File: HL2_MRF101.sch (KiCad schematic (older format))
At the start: 213 parts, among them J1 Antenna, J10 DB1, J2 HL2, J3 RF3, J4 RF1, J5 RCJ-041, J6 50VDC, J7 12V, J8 Fan, J9 HL2_12V, K1 EC2-3NU, K10 EC2-3NU, K11 EC2-3NU, K12 EC2-3NU, K13 EC2-3NU, K2 EC2-3NU, K3 EC2-3NU, K4 EC2-3NU, K5 EC2-3NU, K6 EC2-3NU, K7 EC2-3NU, K8 EC2-3NU, K9 EC2-3NU, Q1 MRF101AN, Q2 2N7002, Q3 IRLML6402, Q4 DTC144E, T1 Coupler, T2 Coupler, T3 744851330, U1 MCP6282E/MS, U2 MAX11613, U3 MCP23008, U4 ULN2003, U5 LM35-NEB, U6 MCP4561, U7 INA193

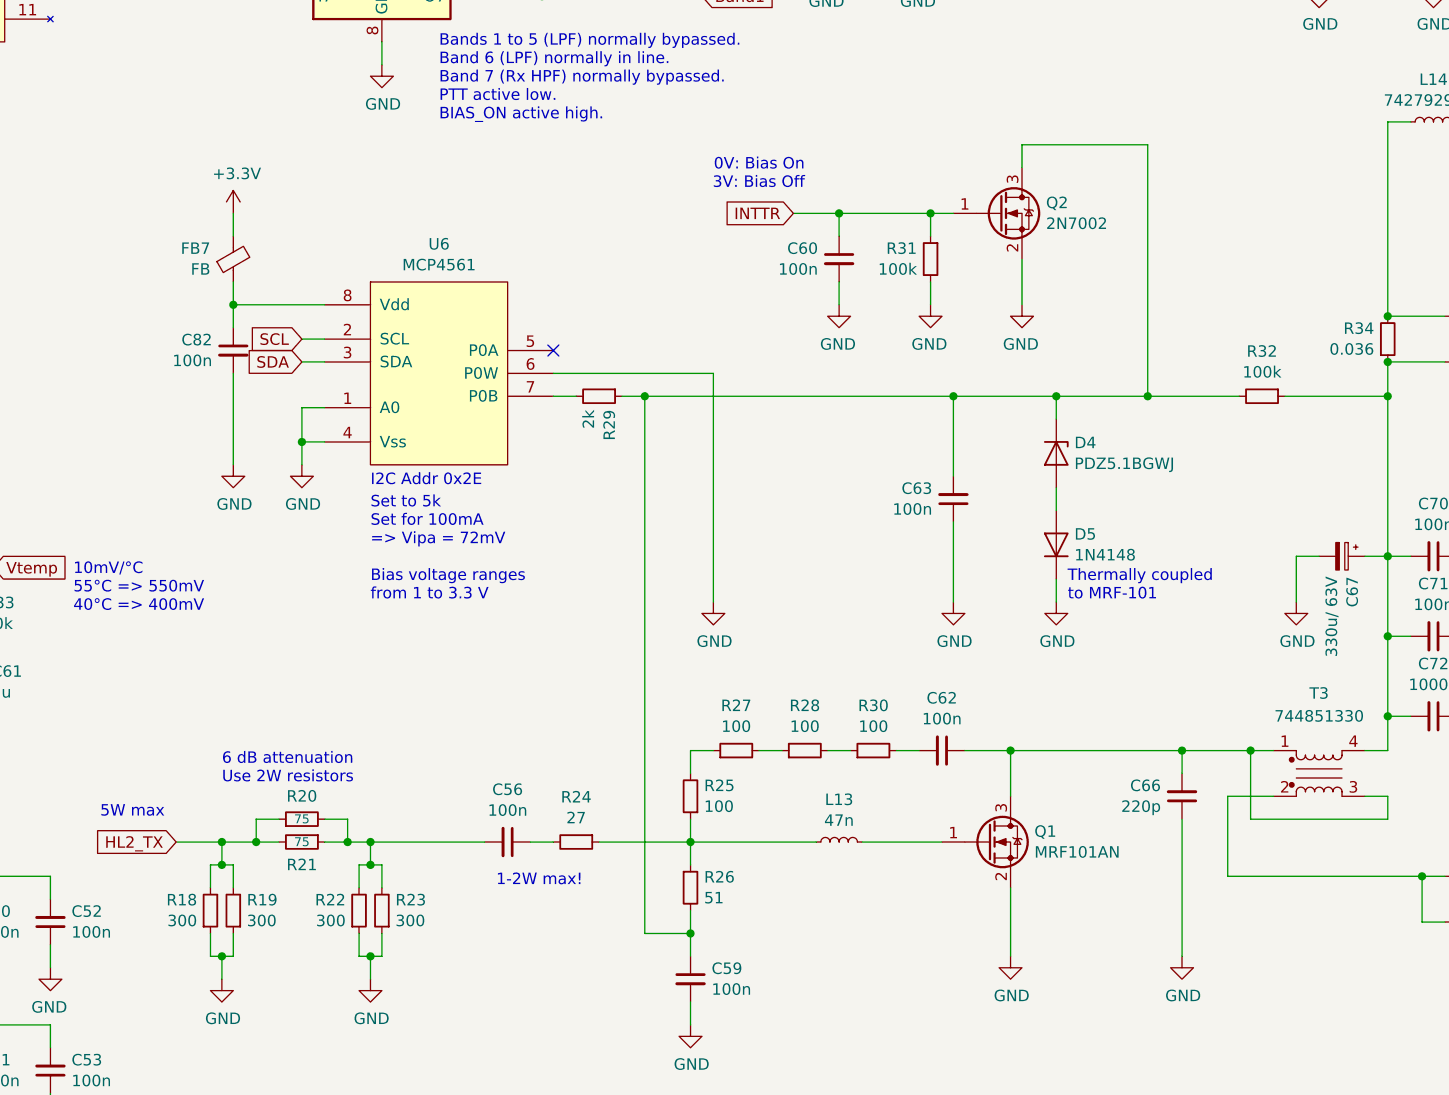
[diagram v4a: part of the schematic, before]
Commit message: Reworked bias circuit, again.
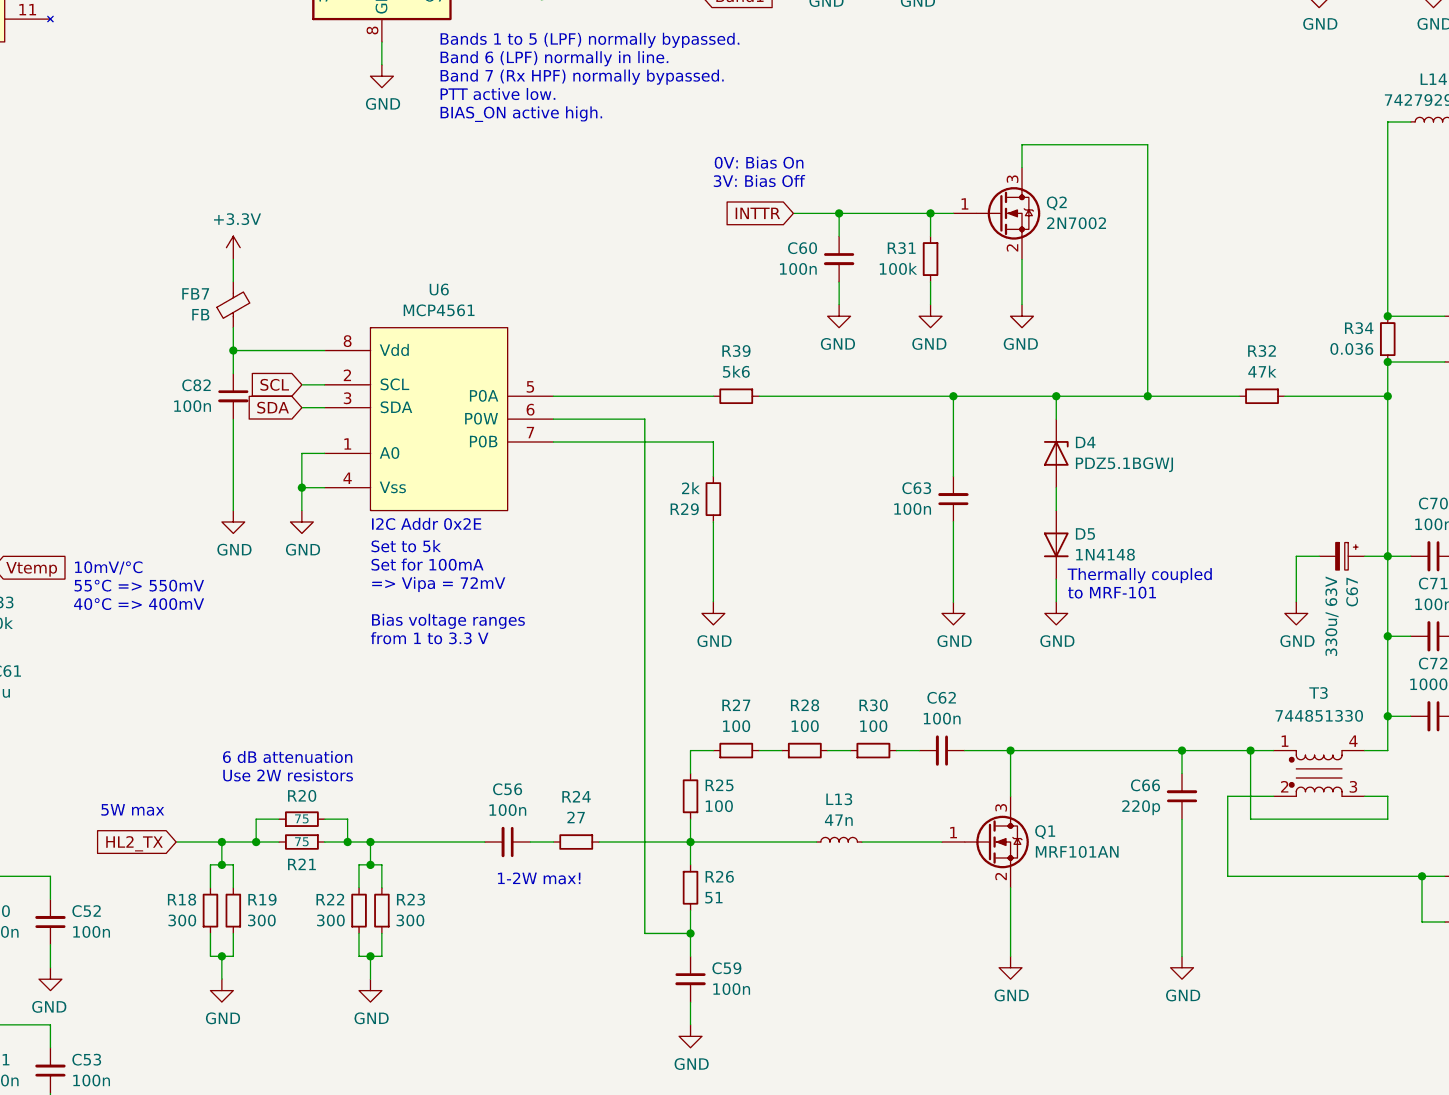
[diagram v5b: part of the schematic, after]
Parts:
- added R39: 5k6, Resistor_SMD:R_0805_2012Metric, symbol HL2_MRF101-rescue:R_Small-Device
- R32: value 100k -> 47k
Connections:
- net GND: now also R29.1; no longer U6.6 (P0W)
- net at C63.2, D4.1 (K), Q2.3 (D)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: now also R39.1; no longer C59.1, R26.2, R29.1
- net at U6.5 (P0A): now also R39.2
- new net: C59.1, R26.2, U6.6 (P0W)
- no-connect marks 10 -> 9
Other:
- moved on the sheet: C82, FB7, R29, U6
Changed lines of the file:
@@
 P 13450 3950
 F 0 "R32" V 13254 3950 50  0000 C CNN
-F 1 "100k" V 13345 3950 50  0000 C CNN
+F 1 "47k" V 13345 3950 50  0000 C CNN
 F 2 "Resistor_SMD:R_0805_2012Metric" H 13450 3950 50  0001 C CNN
 F 3 "~" H 13450 3950 50  0001 C CNN
@@
 Wire Wire Line
 	13900 4650 14000 4650
-Text Notes 9550 4850 0    50   ~ 0
+Text Notes 9550 5050 0    50   ~ 0
 Set to 5k\nSet for 100mA\n=> Vipa = 72mV\n\nBias voltage ranges\nfrom 1 to 3.3 V
 Text Notes 10100 6100 0    50   ~ 0
@@
 L HL2-MRF101:MCP4561 U6
 U 1 1 6200A830
-P 9850 3850
-F 0 "U6" H 9850 4415 50  0000 C CNN
-F 1 "MCP4561" H 9850 4324 50  0000 C CNN
-F 2 "Package_SO:MSOP-8_3x3mm_P0.65mm" H 9650 5500 50  0001 C CNN
-F 3 "" H 9650 5500 50  0001 C CNN
-	1    9850 3850
+P 9850 4050
+F 0 "U6" H 9850 4615 50  0000 C CNN
+F 1 "MCP4561" H 9850 4524 50  0000 C CNN
+F 2 "Package_SO:MSOP-8_3x3mm_P0.65mm" H 9650 5700 50  0001 C CNN
+F 3 "" H 9650 5700 50  0001 C CNN
+	1    9850 4050
 	1    0    0    -1
 $EndComp
-Text GLabel 9250 3700 0    50   Input ~ 0
+Text GLabel 9250 3900 0    50   Input ~ 0
 SCL
-Text GLabel 9250 3800 0    50   Input ~ 0
+Text GLabel 9250 4000 0    50   Input ~ 0
 SDA
 Wire Wire Line
-	9350 3800 9250 3800
+	9350 4000 9250 4000
 Wire Wire Line
-	9350 3700 9250 3700
+	9350 3900 9250 3900
 Wire Wire Line
-	8950 3550 9350 3550
+	8950 3750 9350 3750
 $Comp
 L HL2_MRF101-rescue:C_Small-Device C82
 U 1 1 6244D31F
-P 8950 3750
-F 0 "C82" H 9042 3796 50  0000 L CNN
-F 1 "100n" H 9042 3705 50  0000 L CNN
-F 2 "Capacitor_SMD:C_0805_2012Metric" H 8950 3750 50  0001 C CNN
-F 3 "~" H 8950 3750 50  0001 C CNN
-	1    8950 3750
+P 8950 3950
+F 0 "C82" H 9042 3996 50  0000 L CNN
+F 1 "100n" H 9042 3905 50  0000 L CNN
+F 2 "Capacitor_SMD:C_0805_2012Metric" H 8950 3950 50  0001 C CNN
+F 3 "~" H 8950 3950 50  0001 C CNN
+	1    8950 3950
 	-1   0    0    -1
 $EndComp
 Wire Wire Line
-	8950 3550 8950 3650
+	8950 3750 8950 3850
 $Comp
 L power:+3.3V #PWR0104
 U 1 1 624EB2A7
-P 8950 3150
-F 0 "#PWR0104" H 8950 3000 50  0001 C CNN
-F 1 "+3.3V" H 8965 3323 50  0000 C CNN
-F 2 "" H 8950 3150 50  0001 C CNN
-F 3 "" H 8950 3150 50  0001 C CNN
-	1    8950 3150
+P 8950 3350
+F 0 "#PWR0104" H 8950 3200 50  0001 C CNN
+F 1 "+3.3V" H 8965 3523 50  0000 C CNN
+F 2 "" H 8950 3350 50  0001 C CNN
+F 3 "" H 8950 3350 50  0001 C CNN
+	1    8950 3350
 	1    0    0    -1
 $EndComp
@@
 L HL2_MRF101-rescue:Ferrite_Bead_Small-device FB7
 U 1 1 624EB2B1
-P 8950 3350
-F 0 "FB7" H 8850 3304 50  0000 R CNN
-F 1 "FB" H 8850 3395 50  0000 R CNN
-F 2 "Inductor_SMD:L_0805_2012Metric" V 8880 3350 50  0001 C CNN
-F 3 "~" H 8950 3350 50  0001 C CNN
-	1    8950 3350
+P 8950 3550
+F 0 "FB7" H 8850 3504 50  0000 R CNN
+F 1 "FB" H 8850 3595 50  0000 R CNN
+F 2 "Inductor_SMD:L_0805_2012Metric" V 8880 3550 50  0001 C CNN
+F 3 "~" H 8950 3550 50  0001 C CNN
+	1    8950 3550
 	1    0    0    1
 $EndComp
 Wire Wire Line
-	8950 3150 8950 3250
+	8950 3350 8950 3450
 Wire Wire Line
-	8950 3450 8950 3550
+	8950 3650 8950 3750
 $Comp
 L power:GND #PWR0112
 U 1 1 62627FA1
-P 9250 4250
-F 0 "#PWR0112" H 9250 4000 50  0001 C CNN
-F 1 "GND" H 9255 4077 50  0000 C CNN
-F 2 "" H 9250 4250 50  0001 C CNN
-F 3 "" H 9250 4250 50  0001 C CNN
-	1    9250 4250
+P 9250 4450
+F 0 "#PWR0112" H 9250 4200 50  0001 C CNN
+F 1 "GND" H 9255 4277 50  0000 C CNN
+F 2 "" H 9250 4450 50  0001 C CNN
+F 3 "" H 9250 4450 50  0001 C CNN
+	1    9250 4450
 	1    0    0    -1
 $EndComp
 Wire Wire Line
-	9350 4150 9250 4150
+	9350 4350 9250 4350
 Wire Wire Line
-	9250 4150 9250 4250
+	9250 4350 9250 4450
 $Comp
 L power:GND #PWR0111
 U 1 1 626C7205
-P 8950 4250
-F 0 "#PWR0111" H 8950 4000 50  0001 C CNN
-F 1 "GND" H 8955 4077 50  0000 C CNN
-F 2 "" H 8950 4250 50  0001 C CNN
-F 3 "" H 8950 4250 50  0001 C CNN
-	1    8950 4250
+P 8950 4450
+F 0 "#PWR0111" H 8950 4200 50  0001 C CNN
+F 1 "GND" H 8955 4277 50  0000 C CNN
+F 2 "" H 8950 4450 50  0001 C CNN
+F 3 "" H 8950 4450 50  0001 C CNN
+	1    8950 4450
 	1    0    0    -1
 $EndComp
 Wire Wire Line
-	8950 3850 8950 4250
-Text Notes 9550 4350 0    50   ~ 0
+	8950 4050 8950 4450
+Text Notes 9550 4550 0    50   ~ 0
 I2C Addr 0x2E
 Wire Wire Line
-	9350 4000 9250 4000
+	9350 4200 9250 4200
 Wire Wire Line
-	9250 4000 9250 4150
-Connection ~ 9250 4150
-Connection ~ 8950 3550
+	9250 4200 9250 4350
+Connection ~ 9250 4350
+Connection ~ 8950 3750
 Text Notes 14450 3550 0    50   ~ 0
 4A => 144mV
@@
 L HL2_MRF101-rescue:R_Small-Device R29
 U 1 1 5E0BF37A
-P 10550 3950
-F 0 "R29" H 10609 3996 50  0000 L CNN
-F 1 "2k" H 10609 3905 50  0000 L CNN
-F 2 "Resistor_SMD:R_0805_2012Metric" H 10550 3950 50  0001 C CNN
-F 3 "~" H 10550 3950 50  0001 C CNN
-	1    10550 3950
-	0    1    1    0
+P 11050 4400
+F 0 "R29" H 11109 4446 50  0000 L CNN
+F 1 "2k" H 11109 4355 50  0000 L CNN
+F 2 "Resistor_SMD:R_0805_2012Metric" H 11050 4400 50  0001 C CNN
+F 3 "~" H 11050 4400 50  0001 C CNN
+	1    11050 4400
+	-1   0    0    1
 $EndComp
 Text GLabel 1000 8950 2    50   Input ~ 0
@@
 Wire Wire Line
 	1750 10350 1850 10350
-NoConn ~ 10350 3750
-Wire Wire Line
-	10350 3950 10450 3950
-Wire Wire Line
-	10750 6300 10750 3950
-Wire Wire Line
-	10750 3950 10650 3950
-Wire Wire Line
-	10750 3950 12100 3950
-Connection ~ 10750 3950
-Connection ~ 12100 3950
-Wire Wire Line
-	10350 3850 11050 3850
-Wire Wire Line
-	11050 3850 11050 4850
 $Comp
-L power:GND #PWR?
+L power:GND #PWR061
 U 1 1 63E68A3C
 P 11050 4850
-F 0 "#PWR?" H 11050 4600 50  0001 C CNN
+F 0 "#PWR061" H 11050 4600 50  0001 C CNN
 F 1 "GND" H 11055 4677 50  0000 C CNN
 F 2 "" H 11050 4850 50  0001 C CNN
@@
 	1    0    0    -1
 $EndComp
+$Comp
+L HL2_MRF101-rescue:R_Small-Device R39
+U 1 1 5E3E3EE6
+P 11150 3950
+F 0 "R39" V 10954 3950 50  0000 C CNN
+F 1 "5k6" V 11045 3950 50  0000 C CNN
+F 2 "Resistor_SMD:R_0805_2012Metric" H 11150 3950 50  0001 C CNN
+F 3 "~" H 11150 3950 50  0001 C CNN
+	1    11150 3950
+	0    1    1    0
+$EndComp
+Wire Wire Line
+	10350 4150 11050 4150
+Wire Wire Line
+	11050 4150 11050 4300
+Wire Wire Line
+	11050 4500 11050 4850
+Wire Wire Line
+	11250 3950 12100 3950
+Connection ~ 12100 3950
+Wire Wire Line
+	11050 3950 10350 3950
+Wire Wire Line
+	10750 6300 10750 4050
+Wire Wire Line
+	10750 4050 10350 4050
 $EndSCHEMATC

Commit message: Impedance Adjustment started
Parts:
- added F?: Fuse_Small, symbol Device:Fuse_Small
- C84, C85: symbol device:C_Small -> HL2_MRF101-rescue:C_Small-device
- D6: symbol diode:1N4148W -> HL2_MRF101-rescue:1N4148W-diode
- FB10, FB11, FB12, FB13, FB14, FB15, FB16, FB17, FB18, FB9: symbol device:Ferrite_Bead_Small -> HL2_MRF101-rescue:Ferrite_Bead_Small-device
- J10: symbol conn:Conn_01x06 -> HL2_MRF101-rescue:Conn_01x06-conn
- Q3: symbol device:Q_PMOS_GSD -> HL2_MRF101-rescue:Q_PMOS_GSD-device
- Q4: symbol transistors:DTC144E -> HL2_MRF101-rescue:DTC144E-transistors
- R10, R5: value 56k -> 100k
- R11, R4: value 100k -> 56k
- R16, R17, R36, R37, R38: symbol device:R_Small -> HL2_MRF101-rescue:R_Small-device
- U2: value MAX11613 -> MAX11645
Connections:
- net at J6.1 (Pin_1): now also F?.1; no longer L14.1
- new net: F?.2, L14.1
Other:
- moved on the sheet: L14
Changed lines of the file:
@@
 P 12400 8200
 F 0 "R10" V 12204 8200 50  0000 C CNN
-F 1 "56k" V 12295 8200 50  0000 C CNN
+F 1 "100k" V 12295 8200 50  0000 C CNN
 F 2 "Resistor_SMD:R_0805_2012Metric" H 12400 8200 50  0001 C CNN
 F 3 "~" H 12400 8200 50  0001 C CNN
@@
 P 12600 8400
 F 0 "R11" H 12541 8354 50  0000 R CNN
-F 1 "100k" H 12541 8445 50  0000 R CNN
+F 1 "56k" H 12541 8445 50  0000 R CNN
 F 2 "Resistor_SMD:R_0805_2012Metric" H 12600 8400 50  0001 C CNN
 F 3 "~" H 12600 8400 50  0001 C CNN
@@
 P 9350 8200
 F 0 "R5" V 9154 8200 50  0000 C CNN
-F 1 "56k" V 9245 8200 50  0000 C CNN
+F 1 "100k" V 9245 8200 50  0000 C CNN
 F 2 "Resistor_SMD:R_0805_2012Metric" H 9350 8200 50  0001 C CNN
 F 3 "~" H 9350 8200 50  0001 C CNN
@@
 P 9150 8400
 F 0 "R4" H 9091 8354 50  0000 R CNN
-F 1 "100k" H 9091 8445 50  0000 R CNN
+F 1 "56k" H 9091 8445 50  0000 R CNN
 F 2 "Resistor_SMD:R_0805_2012Metric" H 9150 8400 50  0001 C CNN
 F 3 "~" H 9150 8400 50  0001 C CNN
@@
 	14550 2750 14300 2750
 $Comp
-L HL2_MRF101-rescue:L_Small-Device L14
-U 1 1 63DACD97
-P 14200 2750
-F 0 "L14" V 14385 2750 50  0000 C CNN
-F 1 "7427929112" V 14294 2750 50  0000 C CNN
-F 2 "n2adr:SignalCommunications-WE-PF_7427929XXX" H 14200 2750 50  0001 C CNN
-F 3 "~" H 14200 2750 50  0001 C CNN
-	1    14200 2750
-	0    1    -1   0
-$EndComp
-$Comp
 L HL2_MRF101-rescue:Conn_01x02-Connector_Generic J6
 U 1 1 63DAB1DA
@@
 	1    0    0    -1
 $EndComp
-Wire Wire Line
-	14000 2750 14100 2750
 $Comp
 L power:GND #PWR0113
@@
 P 14700 1600
 F 0 "U2" H 14700 1187 50  0000 C CNN
-F 1 "MAX11613" H 14700 1278 49  0000 C CNN
+F 1 "MAX11645" H 14700 1278 49  0000 C CNN
 F 2 "n2adr:MAX11613" H 14700 1125 50  0001 C CNN
 F 3 "DOCUMENTATION" H 14700 1300 50  0001 C CNN
@@
 	14000 3950 14000 4650
 Connection ~ 14000 3950
-Wire Wire Line
-	14000 3600 14000 2750
-Connection ~ 14000 3600
 $Comp
-L device:Ferrite_Bead_Small FB10
+L HL2_MRF101-rescue:Ferrite_Bead_Small-device FB10
 U 1 1 5E39790B
 P 5950 1600
@@
 	6050 1600 6150 1600
 $Comp
-L device:Ferrite_Bead_Small FB12
+L HL2_MRF101-rescue:Ferrite_Bead_Small-device FB12
 U 1 1 5E4400FC
 P 5950 2900
@@
 	6150 2900 6050 2900
 $Comp
-L device:Ferrite_Bead_Small FB14
+L HL2_MRF101-rescue:Ferrite_Bead_Small-device FB14
 U 1 1 5E4E8E6D
 P 5950 4200
@@
 	6050 4200 6150 4200
 $Comp
-L device:Ferrite_Bead_Small FB16
+L HL2_MRF101-rescue:Ferrite_Bead_Small-device FB16
 U 1 1 5E5925AB
 P 5950 5500
@@
 	6150 5500 6050 5500
 $Comp
-L device:Ferrite_Bead_Small FB18
+L HL2_MRF101-rescue:Ferrite_Bead_Small-device FB18
 U 1 1 5E63C014
 P 5950 6800
@@
 Connection ~ 5450 6700
 $Comp
-L device:Ferrite_Bead_Small FB17
+L HL2_MRF101-rescue:Ferrite_Bead_Small-device FB17
 U 1 1 5E9A3A71
 P 1000 6800
@@
 	800  6800 900  6800
 $Comp
-L device:Ferrite_Bead_Small FB15
+L HL2_MRF101-rescue:Ferrite_Bead_Small-device FB15
 U 1 1 5EAFA782
 P 1000 5500
@@
 	800  5500 900  5500
 $Comp
-L device:Ferrite_Bead_Small FB13
+L HL2_MRF101-rescue:Ferrite_Bead_Small-device FB13
 U 1 1 5ECFC9ED
 P 1000 4200
@@
 	800  4200 900  4200
 $Comp
-L device:Ferrite_Bead_Small FB11
+L HL2_MRF101-rescue:Ferrite_Bead_Small-device FB11
 U 1 1 5EE55DAE
 P 1000 2900
@@
 	800  2900 900  2900
 $Comp
-L device:Ferrite_Bead_Small FB9
+L HL2_MRF101-rescue:Ferrite_Bead_Small-device FB9
 U 1 1 5F107944
 P 1000 1600
@@
 	900  9950 2950 9950
 $Comp
-L device:R_Small R36
+L HL2_MRF101-rescue:R_Small-device R36
 U 1 1 5F471469
 P 1950 10350
@@
 $EndComp
 $Comp
-L device:R_Small R38
+L HL2_MRF101-rescue:R_Small-device R38
 U 1 1 5F4733D9
 P 2150 10550
@@
 $EndComp
 $Comp
-L device:R_Small R37
+L HL2_MRF101-rescue:R_Small-device R37
 U 1 1 5F47390A
 P 1750 10550
@@
 FWD_DET
 $Comp
-L transistors:DTC144E Q4
+L HL2_MRF101-rescue:DTC144E-transistors Q4
 U 1 1 5FE35199
 P 9550 10400
@@
 $EndComp
 $Comp
-L device:Q_PMOS_GSD Q3
+L HL2_MRF101-rescue:Q_PMOS_GSD-device Q3
 U 1 1 5FF9F9AC
 P 10450 10100
@@
 	8450 1500 8450 1400
 $Comp
-L device:C_Small C85
+L HL2_MRF101-rescue:C_Small-device C85
 U 1 1 604A1A52
 P 10550 10600
@@
 	10150 10100 10250 10100
 $Comp
-L device:C_Small C84
+L HL2_MRF101-rescue:C_Small-device C84
 U 1 1 60D3909C
 P 10150 10400
@@
 Connection ~ 10150 10100
 $Comp
-L device:R_Small R17
+L HL2_MRF101-rescue:R_Small-device R17
 U 1 1 60EABC72
 P 9950 10100
@@
 	10150 10500 10150 10800
 $Comp
-L device:R_Small R16
+L HL2_MRF101-rescue:R_Small-device R16
 U 1 1 616A8DF0
 P 10350 9800
@@
 $EndComp
 $Comp
-L diode:1N4148W D6
+L HL2_MRF101-rescue:1N4148W-diode D6
 U 1 1 618D1626
 P 10850 10600
@@
 	9650 10100 9850 10100
 $Comp
-L conn:Conn_01x06 J10
+L HL2_MRF101-rescue:Conn_01x06-conn J10
 U 1 1 62688D8F
 P 8400 10400
@@
 Wire Wire Line
 	10750 4050 10350 4050
+$Comp
+L Device:Fuse_Small F?
+U 1 1 5E4932D6
+P 14200 2750
+F 0 "F?" H 14200 2565 50  0000 C CNN
+F 1 "Fuse_Small" H 14200 2656 50  0000 C CNN
+F 2 "" H 14200 2750 50  0001 C CNN
+F 3 "~" H 14200 2750 50  0001 C CNN
+	1    14200 2750
+	-1   0    0    1
+$EndComp
+$Comp
+L HL2_MRF101-rescue:L_Small-Device L14
+U 1 1 63DACD97
+P 14000 3050
+F 0 "L14" V 14185 3050 50  0000 C CNN
+F 1 "7427929112" V 14094 3050 50  0000 C CNN
+F 2 "n2adr:SignalCommunications-WE-PF_7427929XXX" H 14000 3050 50  0001 C CNN
+F 3 "~" H 14000 3050 50  0001 C CNN
+	1    14000 3050
+	-1   0    0    -1
+$EndComp
+Wire Wire Line
+	14100 2750 14000 2750
+Wire Wire Line
+	14000 2750 14000 2950
+Wire Wire Line
+	14000 3150 14000 3600
+Connection ~ 14000 3600
 $EndSCHEMATC

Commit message: Updated FET circuit
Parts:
- removed F?: Fuse_Small, symbol Device:Fuse_Small
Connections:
- net Vipa: now also C80.2, U2.1 (AIN0); no longer C79.2, U2.2 (AIN1)
- net Vtemp: now also C79.2, U2.2 (AIN1); no longer C80.2, U2.1 (AIN0)
- net at J6.1 (Pin_1): now also L14.1
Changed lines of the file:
@@
 Wire Wire Line
 	14550 2850 14450 2850
-Wire Wire Line
-	14550 2750 14300 2750
 $Comp
 L HL2_MRF101-rescue:Conn_01x02-Connector_Generic J6
@@
 	1    0    0    1
 $EndComp
-Text GLabel 13600 1650 0    50   Input ~ 0
+Text GLabel 14100 1750 0    50   Input ~ 0
 Vipa
 $Comp
@@
 	1    0    0    1
 $EndComp
-Text GLabel 14100 1750 0    50   Input ~ 0
+Text GLabel 13600 1650 0    50   Input ~ 0
 Vtemp
 Wire Wire Line
@@
 	10750 4050 10350 4050
 $Comp
-L Device:Fuse_Small F?
-U 1 1 5E4932D6
-P 14200 2750
-F 0 "F?" H 14200 2565 50  0000 C CNN
-F 1 "Fuse_Small" H 14200 2656 50  0000 C CNN
-F 2 "" H 14200 2750 50  0001 C CNN
-F 3 "~" H 14200 2750 50  0001 C CNN
-	1    14200 2750
-	-1   0    0    1
-$EndComp
-$Comp
 L HL2_MRF101-rescue:L_Small-Device L14
 U 1 1 63DACD97
@@
 $EndComp
 Wire Wire Line
-	14100 2750 14000 2750
-Wire Wire Line
 	14000 2750 14000 2950
 Wire Wire Line
 	14000 3150 14000 3600
 Connection ~ 14000 3600
+Wire Wire Line
+	14000 2750 14550 2750
 $EndSCHEMATC

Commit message: Revision 0.2
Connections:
- net Vipa: now also C79.2, U2.2 (AIN1); no longer C80.2, U2.1 (AIN0)
- net Vtemp: now also C80.2, U2.1 (AIN0); no longer C79.2, U2.2 (AIN1)
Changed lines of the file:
@@
 	1    0    0    1
 $EndComp
-Text GLabel 14100 1750 0    50   Input ~ 0
+Text GLabel 13600 1650 0    50   Input ~ 0
 Vipa
 $Comp
@@
 	1    0    0    1
 $EndComp
-Text GLabel 13600 1650 0    50   Input ~ 0
+Text GLabel 14100 1750 0    50   Input ~ 0
 Vtemp
 Wire Wire Line
